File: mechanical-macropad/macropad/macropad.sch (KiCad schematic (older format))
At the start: 84 parts, among them J1 USB_B_Micro, J2 AVR-ISP-6, K1 KEYSW, K10 KEYSW, K11 KEYSW, K12 KEYSW, K13 KEYSW, K14 KEYSW, K15 KEYSW, K16 KEYSW, K17 KEYSW, K18 KEYSW, K19 KEYSW, K2 KEYSW, K20 KEYSW, K21 KEYSW, K22 KEYSW, K23 KEYSW, K24 KEYSW, K25 KEYSW, K26 KEYSW, K27 KEYSW, K28 KEYSW, K3 KEYSW, K4 KEYSW, K5 KEYSW, K6 KEYSW, K7 KEYSW, K8 KEYSW, K9 KEYSW, SW1 SW_Push, U1 ATMEGA32U4, X1 XTAL_GND

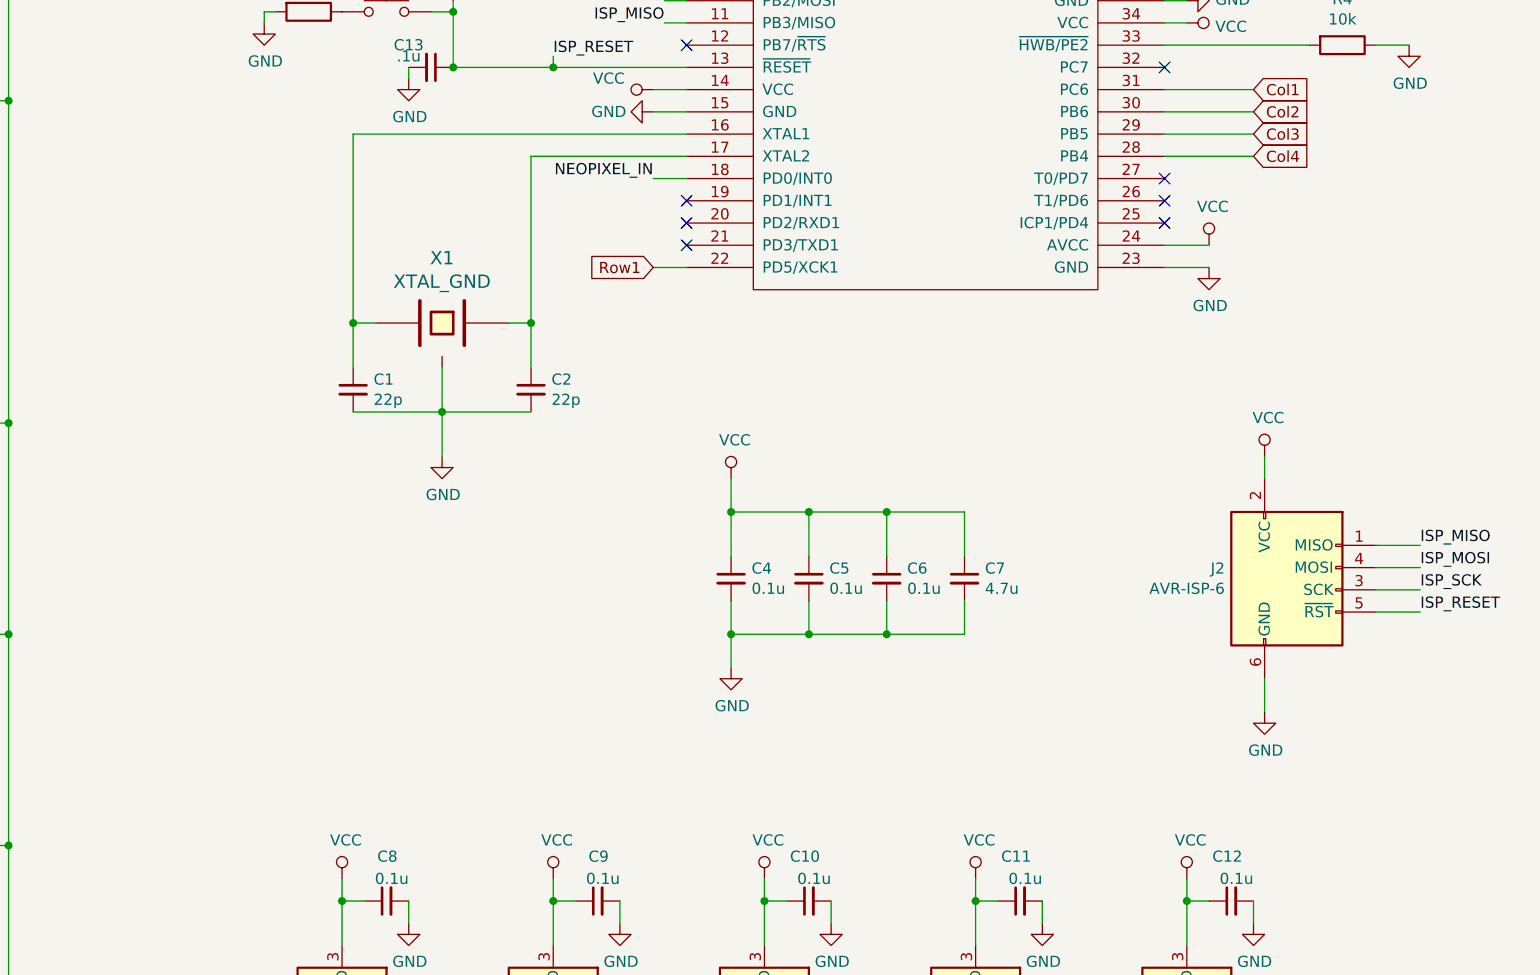
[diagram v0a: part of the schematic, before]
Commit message: Add debug LED, debug pads, reroute
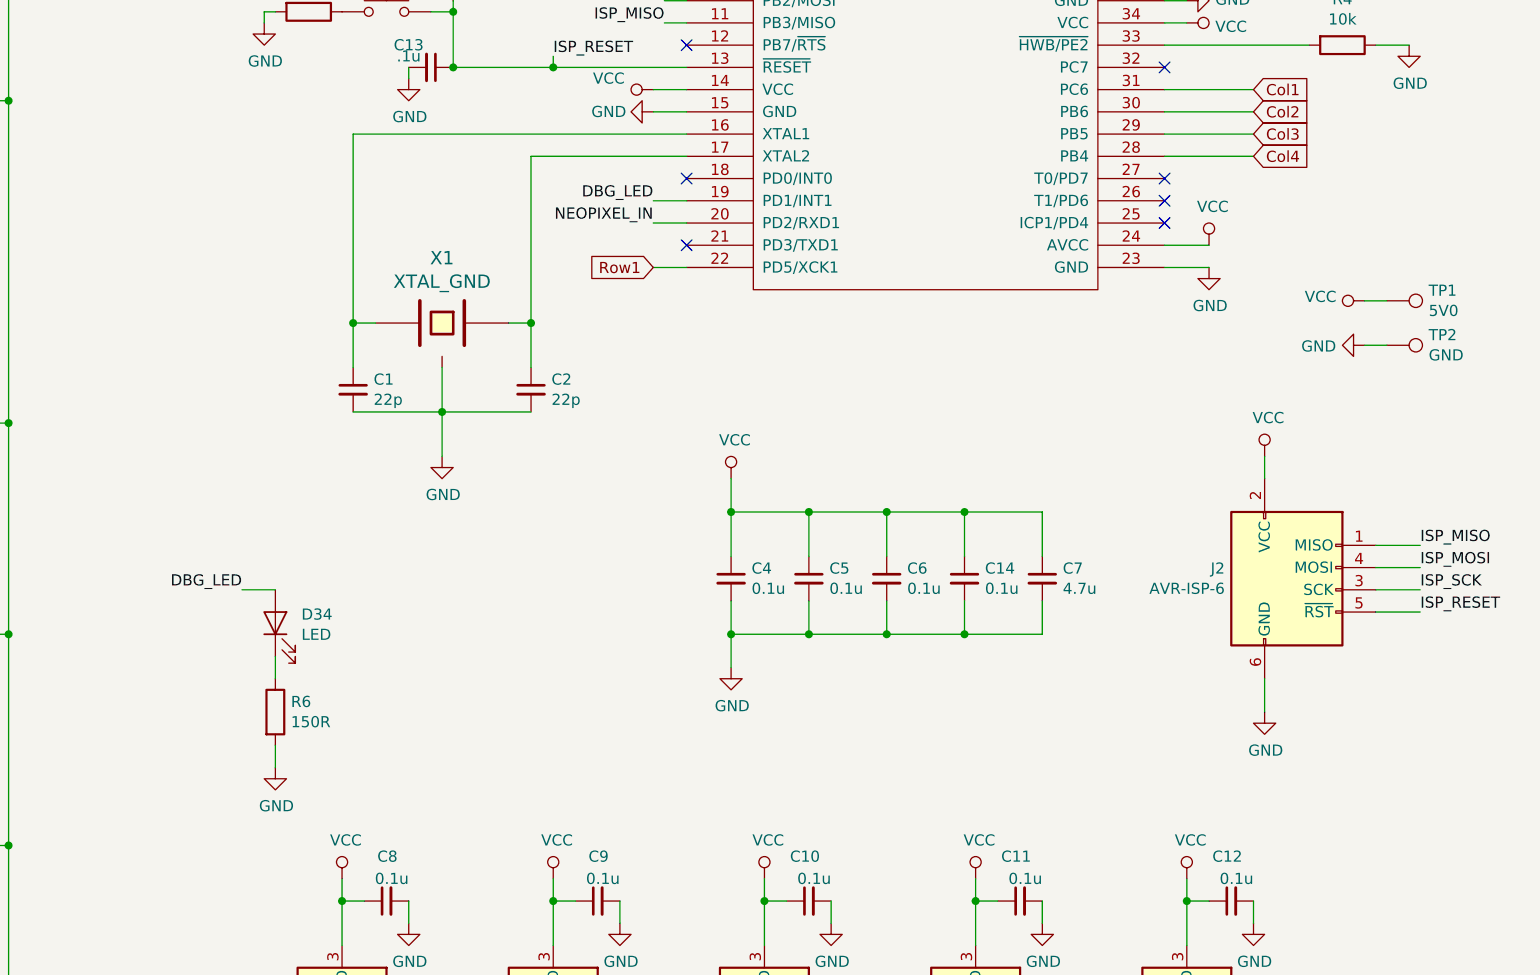
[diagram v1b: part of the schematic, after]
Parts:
- added C14: 0.1u, Capacitor_SMD:C_0805_2012Metric_Pad1.15x1.40mm_HandSolder, symbol Device:C_Small
- added D34: LED, LED_SMD:LED_0805_2012Metric_Pad1.15x1.40mm_HandSolder, symbol Device:LED
- added R6: 150R, Resistor_SMD:R_0805_2012Metric_Pad1.15x1.40mm_HandSolder, symbol Device:R
- added TP1: 5V0, TestPoint:TestPoint_Pad_D4.0mm, symbol Connector:TestPoint
- added TP2: GND, TestPoint:TestPoint_Pad_D4.0mm, symbol Connector:TestPoint
- J1: footprint keyboard_parts:USB_miniB_hirose_5ST_hand -> Connector_USB:USB_Micro-B_Amphenol_10103594-0001LF_Horizontal
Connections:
- net GND: now also C14.2, R6.2, TP2.1
- net NEOPIXEL_IN: now also U1.20 (PD2/RXD1); no longer U1.18 (PD0/INT0)
- net VCC: now also C14.1, TP1.1
- net DBG_LED: now reaches U1.19 (PD1/INT1)
- net DBG_LED: now also D34.2 (A)
- new net: D34.1 (K), R6.1
- no-connect marks 13 -> 12
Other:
- moved on the sheet: C7
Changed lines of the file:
@@
 L Device:C_Small C7
 U 1 1 5BFCE4AA
-P 8650 6000
-F 0 "C7" H 8742 6046 50  0000 L CNN
-F 1 "4.7u" H 8742 5955 50  0000 L CNN
-F 2 "Capacitor_SMD:C_0805_2012Metric_Pad1.15x1.40mm_HandSolder" H 8650 6000 50  0001 C CNN
-F 3 "~" H 8650 6000 50  0001 C CNN
-	1    8650 6000
-	1    0    0    -1
-$EndComp
-Wire Wire Line
-	8650 5900 8650 5700
+P 9000 6000
+F 0 "C7" H 9092 6046 50  0000 L CNN
+F 1 "4.7u" H 9092 5955 50  0000 L CNN
+F 2 "Capacitor_SMD:C_0805_2012Metric_Pad1.15x1.40mm_HandSolder" H 9000 6000 50  0001 C CNN
+F 3 "~" H 9000 6000 50  0001 C CNN
+	1    9000 6000
+	1    0    0    -1
+$EndComp
+Wire Wire Line
+	9000 5900 9000 5700
 Wire Wire Line
 	8300 5900 8300 5700
@@
 	7600 6250 7950 6250
 Wire Wire Line
-	8650 6250 8650 6100
+	9000 6250 9000 6100
 Wire Wire Line
 	8300 6100 8300 6250
@@
 F 0 "J1" H 5220 2697 50  0000 R CNN
 F 1 "USB_B_Micro" H 5220 2788 50  0000 R CNN
-F 2 "keyboard_parts:USB_miniB_hirose_5ST_hand" H 5600 2750 50  0001 C CNN
+F 2 "Connector_USB:USB_Micro-B_Amphenol_10103594-0001LF_Horizontal" H 5600 2750 50  0001 C CNN
 F 3 "~" H 5600 2750 50  0001 C CNN
 	1    5450 2800
@@
 NoConn ~ 7400 3200
 NoConn ~ 7400 3600
-NoConn ~ 7400 4300
-NoConn ~ 7400 4400
 NoConn ~ 7400 4500
 NoConn ~ 9550 4400
@@
 Wire Wire Line
 	5350 7950 5550 7950
-Text Label 7250 4200 2    50   ~ 0
+Text Label 7250 4400 2    50   ~ 0
 NEOPIXEL_IN
 Wire Wire Line
-	7250 4200 7400 4200
+	7250 4400 7400 4400
 NoConn ~ 5750 2600
 $Comp
@@
 	7250 4600 7400 4600
 NoConn ~ 9550 3700
+NoConn ~ 7400 4200
+$Comp
+L Device:C_Small C14
+U 1 1 5C0797B6
+P 8650 6000
+F 0 "C14" H 8742 6046 50  0000 L CNN
+F 1 "0.1u" H 8742 5955 50  0000 L CNN
+F 2 "Capacitor_SMD:C_0805_2012Metric_Pad1.15x1.40mm_HandSolder" H 8650 6000 50  0001 C CNN
+F 3 "~" H 8650 6000 50  0001 C CNN
+	1    8650 6000
+	1    0    0    -1
+$EndComp
+Wire Wire Line
+	8650 5900 8650 5700
+Wire Wire Line
+	8650 6100 8650 6250
+Wire Wire Line
+	9000 6250 8650 6250
+Connection ~ 8650 6250
+Wire Wire Line
+	8650 5700 9000 5700
+Connection ~ 8650 5700
+Text Label 7250 4300 2    50   ~ 0
+DBG_LED
+Wire Wire Line
+	7250 4300 7400 4300
+Text Label 5400 6050 2    50   ~ 0
+DBG_LED
+$Comp
+L Device:LED D34
+U 1 1 5C0D6E90
+P 5550 6200
+F 0 "D34" V 5589 6083 50  0000 R CNN
+F 1 "LED" V 5498 6083 50  0000 R CNN
+F 2 "LED_SMD:LED_0805_2012Metric_Pad1.15x1.40mm_HandSolder" H 5550 6200 50  0001 C CNN
+F 3 "~" H 5550 6200 50  0001 C CNN
+	1    5550 6200
+	0    -1   -1   0
+$EndComp
+Wire Wire Line
+	5400 6050 5550 6050
+$Comp
+L Device:R R6
+U 1 1 5C0EAA5B
+P 5550 6600
+F 0 "R6" H 5620 6646 50  0000 L CNN
+F 1 "150R" H 5620 6555 50  0000 L CNN
+F 2 "Resistor_SMD:R_0805_2012Metric_Pad1.15x1.40mm_HandSolder" V 5480 6600 50  0001 C CNN
+F 3 "~" H 5550 6600 50  0001 C CNN
+	1    5550 6600
+	1    0    0    -1
+$EndComp
+Wire Wire Line
+	5550 6350 5550 6450
+$Comp
+L power:GND #PWR0124
+U 1 1 5C0FDB6F
+P 5550 6850
+F 0 "#PWR0124" H 5550 6600 50  0001 C CNN
+F 1 "GND" H 5555 6677 50  0000 C CNN
+F 2 "" H 5550 6850 50  0001 C CNN
+F 3 "" H 5550 6850 50  0001 C CNN
+	1    5550 6850
+	1    0    0    -1
+$EndComp
+Wire Wire Line
+	5550 6750 5550 6850
+$Comp
+L Connector:TestPoint TP2
+U 1 1 5C112DD1
+P 10550 4950
+F 0 "TP2" V 10504 5138 50  0000 L CNN
+F 1 "GND" V 10595 5138 50  0000 L CNN
+F 2 "TestPoint:TestPoint_Pad_D4.0mm" H 10750 4950 50  0001 C CNN
+F 3 "~" H 10750 4950 50  0001 C CNN
+	1    10550 4950
+	0    1    1    0
+$EndComp
+$Comp
+L Connector:TestPoint TP1
+U 1 1 5C114C81
+P 10550 4750
+F 0 "TP1" V 10504 4938 50  0000 L CNN
+F 1 "5V0" V 10595 4938 50  0000 L CNN
+F 2 "TestPoint:TestPoint_Pad_D4.0mm" H 10750 4750 50  0001 C CNN
+F 3 "~" H 10750 4750 50  0001 C CNN
+	1    10550 4750
+	0    1    1    0
+$EndComp
+$Comp
+L power:GND #PWR0125
+U 1 1 5C11506B
+P 10450 4950
+F 0 "#PWR0125" H 10450 4700 50  0001 C CNN
+F 1 "GND" V 10455 4822 50  0000 R CNN
+F 2 "" H 10450 4950 50  0001 C CNN
+F 3 "" H 10450 4950 50  0001 C CNN
+	1    10450 4950
+	0    1    1    0
+$EndComp
+$Comp
+L power:VCC #PWR0126
+U 1 1 5C115538
+P 10450 4750
+F 0 "#PWR0126" H 10450 4600 50  0001 C CNN
+F 1 "VCC" V 10468 4877 50  0000 L CNN
+F 2 "" H 10450 4750 50  0001 C CNN
+F 3 "" H 10450 4750 50  0001 C CNN
+	1    10450 4750
+	0    -1   -1   0
+$EndComp
+Wire Wire Line
+	10450 4750 10550 4750
+Wire Wire Line
+	10450 4950 10550 4950
 $EndSCHEMATC

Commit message: Final touches
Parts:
- added H1, H2, H3, H4: MountingHole, MountingHole:MountingHole_3.2mm_M3_Pad, symbol Mechanical:MountingHole_Pad
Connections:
- wire segments 267 -> 271
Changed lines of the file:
@@
 Wire Wire Line
 	10450 4950 10550 4950
+$Comp
+L Mechanical:MountingHole_Pad H1
+U 1 1 5C527352
+P 11650 4600
+F 0 "H1" H 11750 4600 50  0000 L CNN
+F 1 "MountingHole" H 11750 4558 50  0001 L CNN
+F 2 "MountingHole:MountingHole_3.2mm_M3_Pad" H 11650 4600 50  0001 C CNN
+F 3 "~" H 11650 4600 50  0001 C CNN
+	1    11650 4600
+	1    0    0    -1
+$EndComp
+$Comp
+L Mechanical:MountingHole_Pad H2
+U 1 1 5C528E4C
+P 11950 4600
+F 0 "H2" H 12050 4600 50  0000 L CNN
+F 1 "MountingHole" H 12050 4558 50  0001 L CNN
+F 2 "MountingHole:MountingHole_3.2mm_M3_Pad" H 11950 4600 50  0001 C CNN
+F 3 "~" H 11950 4600 50  0001 C CNN
+	1    11950 4600
+	1    0    0    -1
+$EndComp
+$Comp
+L Mechanical:MountingHole_Pad H4
+U 1 1 5C52927D
+P 12550 4600
+F 0 "H4" H 12650 4600 50  0000 L CNN
+F 1 "MountingHole" H 12650 4558 50  0001 L CNN
+F 2 "MountingHole:MountingHole_3.2mm_M3_Pad" H 12550 4600 50  0001 C CNN
+F 3 "~" H 12550 4600 50  0001 C CNN
+	1    12550 4600
+	1    0    0    -1
+$EndComp
+$Comp
+L Mechanical:MountingHole_Pad H3
+U 1 1 5C5295AF
+P 12250 4600
+F 0 "H3" H 12350 4600 50  0000 L CNN
+F 1 "MountingHole" H 12350 4558 50  0001 L CNN
+F 2 "MountingHole:MountingHole_3.2mm_M3_Pad" H 12250 4600 50  0001 C CNN
+F 3 "~" H 12250 4600 50  0001 C CNN
+	1    12250 4600
+	1    0    0    -1
+$EndComp
+Wire Wire Line
+	11650 4700 11950 4700
+Connection ~ 11950 4700
+Wire Wire Line
+	11950 4700 12250 4700
+Connection ~ 12250 4700
+Wire Wire Line
+	12250 4700 12550 4700
+Wire Wire Line
+	12550 4700 12550 4900
+Connection ~ 12550 4700
+$Comp
+L power:GND #PWR06
+U 1 1 5C62D259
+P 12550 4900
+F 0 "#PWR06" H 12550 4650 50  0001 C CNN
+F 1 "GND" H 12555 4727 50  0000 C CNN
+F 2 "" H 12550 4900 50  0001 C CNN
+F 3 "" H 12550 4900 50  0001 C CNN
+	1    12550 4900
+	1    0    0    -1
+$EndComp
 $EndSCHEMATC

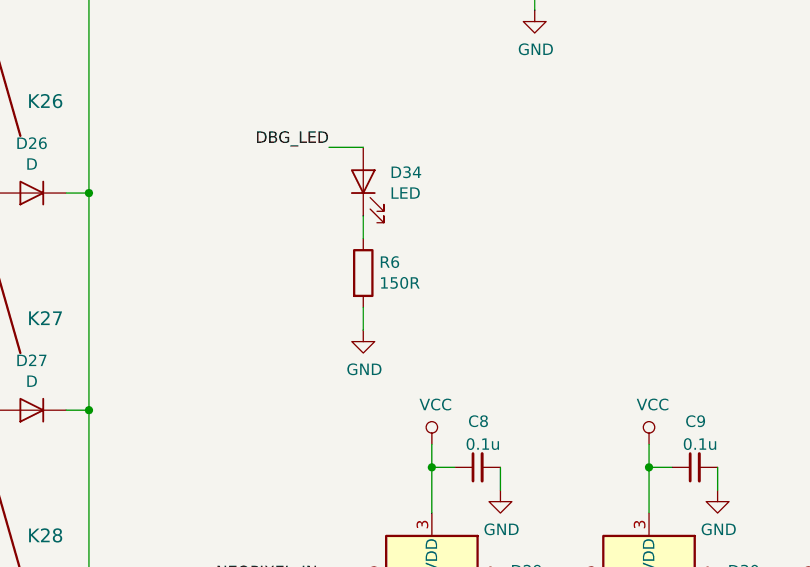
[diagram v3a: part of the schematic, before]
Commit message: Change R6 for a 330R
This both reduces # of components and makes the debug LED less bright.
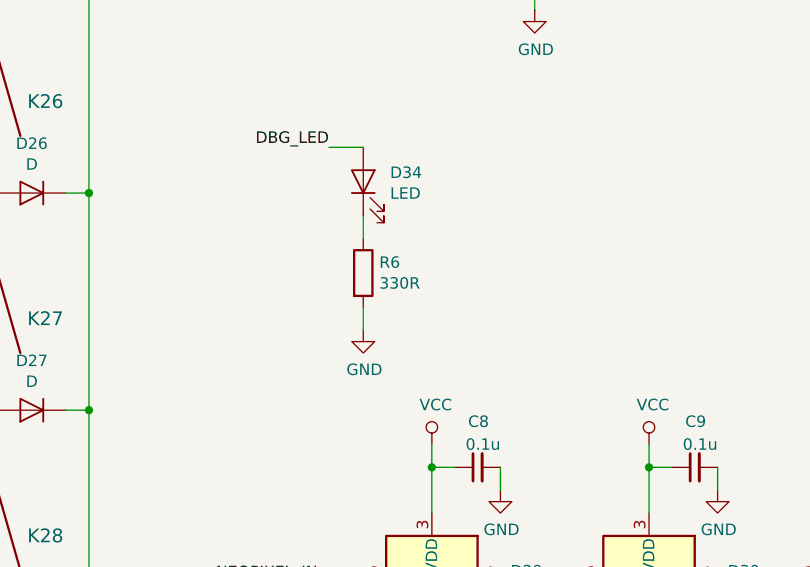
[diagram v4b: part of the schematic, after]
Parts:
- R6: value 150R -> 330R
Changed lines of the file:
@@
 P 5550 6600
 F 0 "R6" H 5620 6646 50  0000 L CNN
-F 1 "150R" H 5620 6555 50  0000 L CNN
+F 1 "330R" H 5620 6555 50  0000 L CNN
 F 2 "Resistor_SMD:R_0805_2012Metric_Pad1.15x1.40mm_HandSolder" V 5480 6600 50  0001 C CNN
 F 3 "~" H 5550 6600 50  0001 C CNN

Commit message: BUG: fix crystal footprint
Somehow it got messed up in the assembled revision. This commit fixes it
in a somewhat slapdash manner. Pull requests on this matter are welcome.
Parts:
- removed X1: XTAL_GND, Crystal:Crystal_SMD_SeikoEpson_FA238-4Pin_3.2x2.5mm_HandSoldering, symbol tmk_keyboard_parts:XTAL_GND
- added Y1: Crystal_GND24, Crystal:Crystal_SMD_SeikoEpson_FA238-4Pin_3.2x2.5mm_HandSoldering, symbol Device:Crystal_GND24
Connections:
- wire segments 271 -> 273
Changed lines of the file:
@@
-$EndComp
-$Comp
-L tmk_keyboard_parts:XTAL_GND X1
-U 1 1 5BFA5C84
-P 6300 4850
-F 0 "X1" H 6300 5142 60  0000 C CNN
-F 1 "XTAL_GND" H 6300 5036 60  0000 C CNN
-F 2 "Crystal:Crystal_SMD_SeikoEpson_FA238-4Pin_3.2x2.5mm_HandSoldering" H 6300 4850 60  0001 C CNN
-F 3 "" H 6300 4850 60  0000 C CNN
-	1    6300 4850
-	-1   0    0    -1
 $EndComp
 $Comp
@@
 	5900 5050 5900 4850
 Wire Wire Line
-	5900 4850 6000 4850
-Wire Wire Line
 	6700 5050 6700 4850
-Wire Wire Line
-	6700 4850 6600 4850
 Wire Wire Line
 	5900 5250 6300 5250
@@
 	1    0    0    -1
 $EndComp
+$Comp
+L Device:Crystal_GND24 Y1
+U 1 1 5C75B6CA
+P 6300 4850
+F 0 "Y1" H 6494 4896 50  0000 L CNN
+F 1 "Crystal_GND24" H 6494 4805 50  0000 L CNN
+F 2 "Crystal:Crystal_SMD_SeikoEpson_FA238-4Pin_3.2x2.5mm_HandSoldering" H 6300 4850 50  0001 C CNN
+F 3 "~" H 6300 4850 50  0001 C CNN
+	1    6300 4850
+	1    0    0    -1
+$EndComp
+Wire Wire Line
+	6450 4850 6700 4850
+Wire Wire Line
+	5900 4850 6150 4850
+$Comp
+L power:GND #PWR0127
+U 1 1 5C7ACB62
+P 6400 4450
+F 0 "#PWR0127" H 6400 4200 50  0001 C CNN
+F 1 "GND" V 6405 4322 50  0000 R CNN
+F 2 "" H 6400 4450 50  0001 C CNN
+F 3 "" H 6400 4450 50  0001 C CNN
+	1    6400 4450
+	0    -1   -1   0
+$EndComp
+Wire Wire Line
+	6300 4650 6300 4450
+Wire Wire Line
+	6300 4450 6400 4450
 $EndSCHEMATC

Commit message: Tie slave select to ground
This is probably pointless, but it guarantees that SPI communication will work.
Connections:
- wire segments 273 -> 274
- no-connect marks 12 -> 11
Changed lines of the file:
@@
 	10000 5450 10000 5550
 NoConn ~ 7400 2500
-NoConn ~ 7400 3200
 NoConn ~ 7400 3600
 NoConn ~ 7400 4500
@@
 Wire Wire Line
 	6300 4450 6400 4450
+$Comp
+L power:GND #PWR?
+U 1 1 5C80B0DF
+P 7350 3200
+F 0 "#PWR?" H 7350 2950 50  0001 C CNN
+F 1 "GND" V 7355 3072 50  0000 R CNN
+F 2 "" H 7350 3200 50  0001 C CNN
+F 3 "" H 7350 3200 50  0001 C CNN
+	1    7350 3200
+	0    1    1    0
+$EndComp
+Wire Wire Line
+	7350 3200 7400 3200
 $EndSCHEMATC
